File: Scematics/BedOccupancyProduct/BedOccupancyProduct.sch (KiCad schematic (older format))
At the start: 6 parts

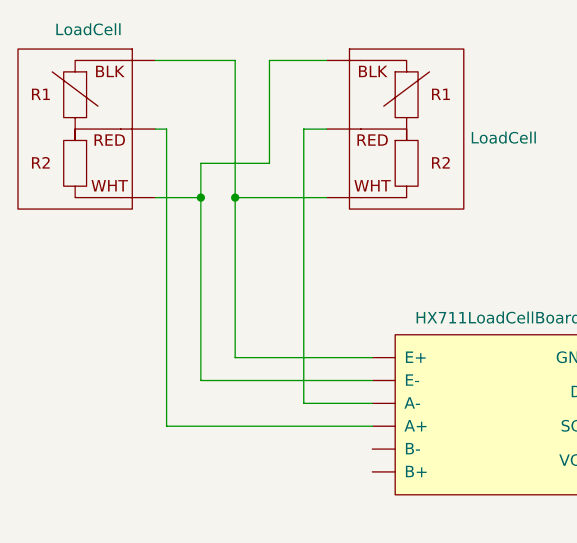
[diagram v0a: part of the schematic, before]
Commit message: code for initial timer and snooze control
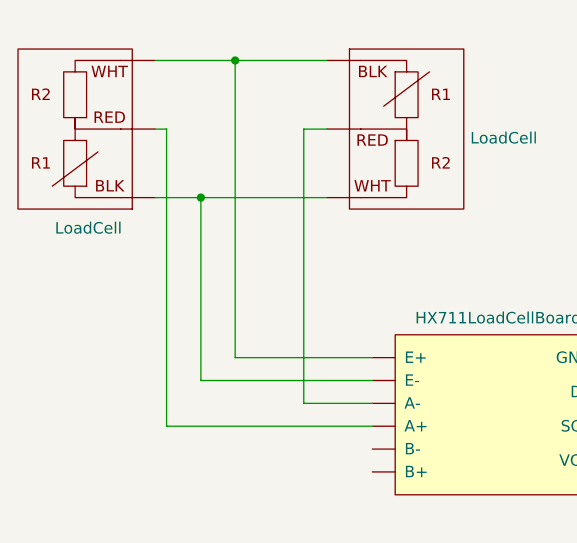
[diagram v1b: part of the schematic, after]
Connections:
- wire segments 39 -> 35
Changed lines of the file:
@@
 $EndComp
-Wire Wire Line
-	1800 1100 2150 1100
-Wire Wire Line
-	2150 1100 2150 1700
-Wire Wire Line
-	2150 1700 2550 1700
-Wire Wire Line
-	2550 1100 2300 1100
-Wire Wire Line
-	2300 1100 2300 1550
-Wire Wire Line
-	2300 1550 2000 1550
-Wire Wire Line
-	2000 1550 2000 1700
-Wire Wire Line
-	2000 1700 1800 1700
-Connection ~ 2000 1700
-Connection ~ 2150 1700
 Wire Wire Line
 	2550 1400 2450 1400
@@
 L alarmclocksystem:LoadCell U?
 U 1 1 5FA06464
-P 1350 900
-F 0 "U?" H 1192 925 50  0001 C CNN
-F 1 "LoadCell" H 1192 834 50  0000 C CNN
-F 2 "" H 1350 900 50  0001 C CNN
-F 3 "" H 1350 900 50  0001 C CNN
-	1    1350 900
-	-1   0    0    -1
+P 1350 1900
+F 0 "U?" H 1192 1925 50  0001 C CNN
+F 1 "LoadCell" H 1192 1834 50  0000 C CNN
+F 2 "" H 1350 1900 50  0001 C CNN
+F 3 "" H 1350 1900 50  0001 C CNN
+	1    1350 1900
+	-1   0    0    1
 $EndComp
 Wire Wire Line
@@
 	2750 2400 2150 2400
 Wire Wire Line
-	2150 1700 2150 2400
-Wire Wire Line
 	2750 2500 2000 2500
-Wire Wire Line
-	2000 1700 2000 2500
 Wire Wire Line
 	2750 2600 2450 2600
@@
 Wire Wire Line
 	6000 3050 7200 3050
+Wire Wire Line
+	1800 1100 2150 1100
+Wire Wire Line
+	1800 1700 2000 1700
+Wire Wire Line
+	2150 2400 2150 1100
+Connection ~ 2150 1100
+Wire Wire Line
+	2150 1100 2550 1100
+Wire Wire Line
+	2000 2500 2000 1700
+Connection ~ 2000 1700
+Wire Wire Line
+	2000 1700 2550 1700
 $EndSCHEMATC

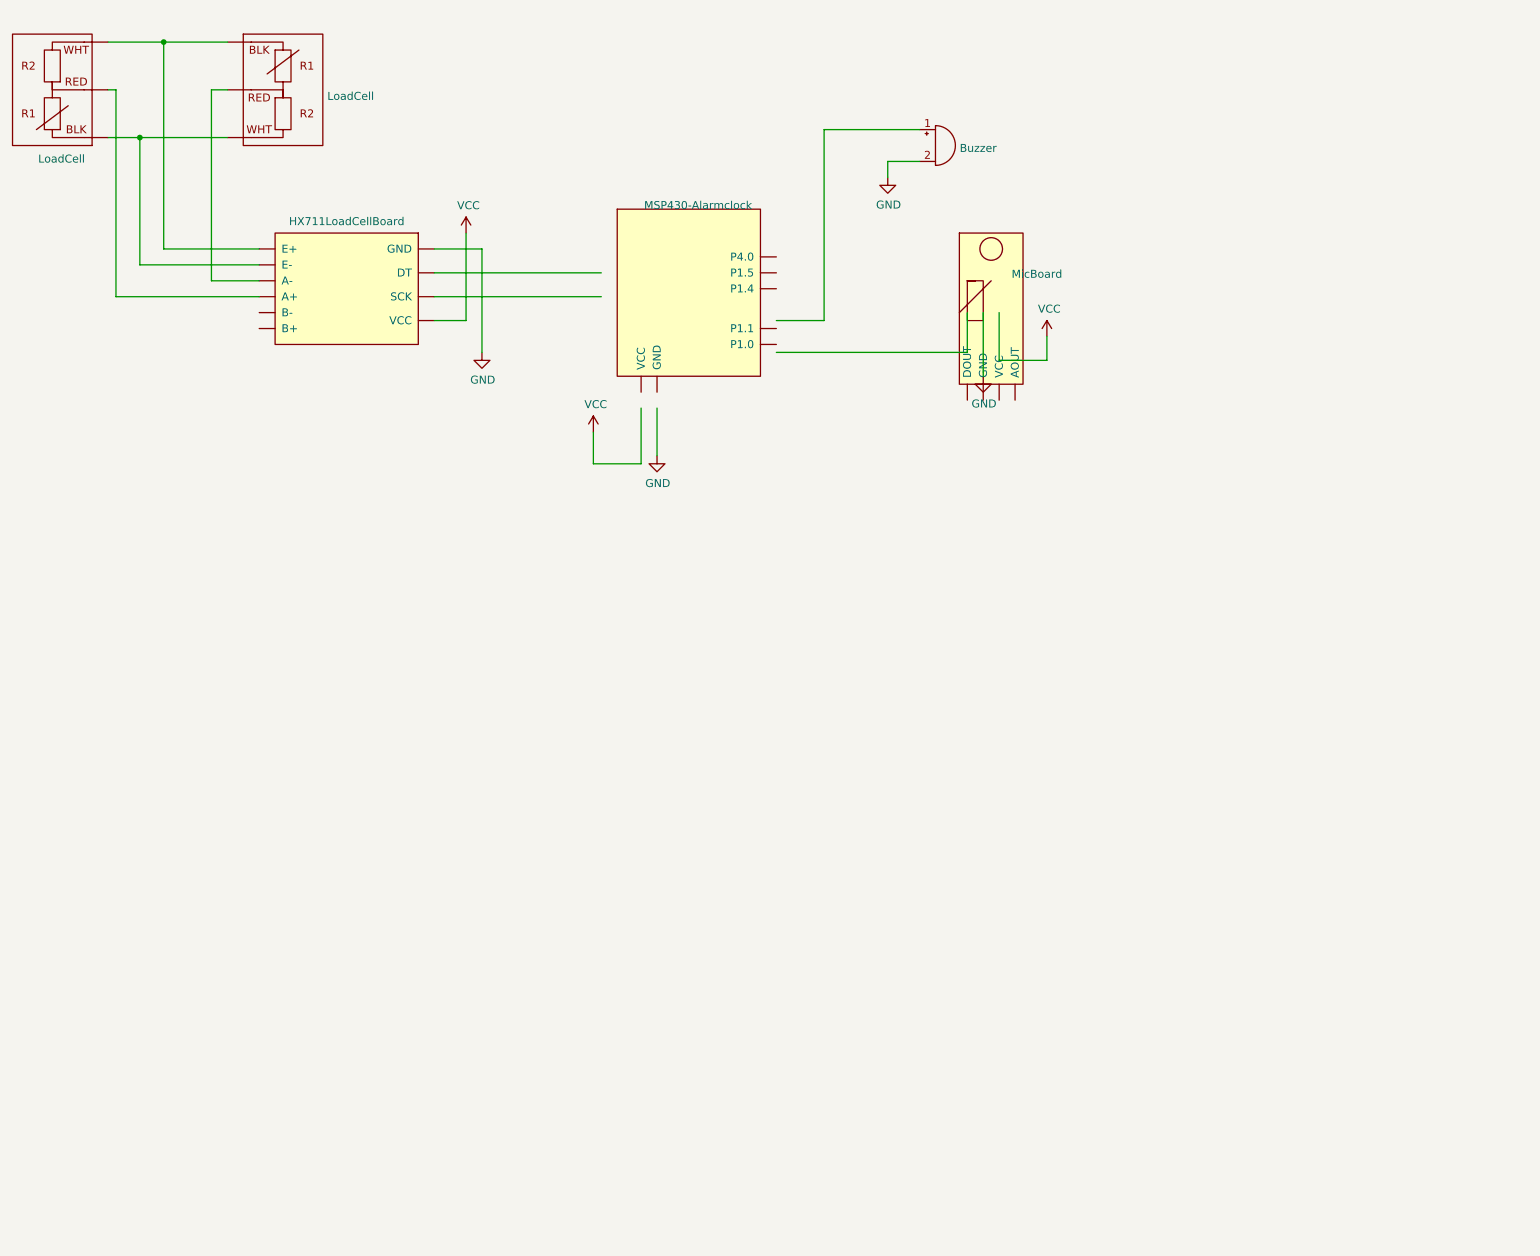
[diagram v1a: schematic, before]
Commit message: timers working with constant buzzer
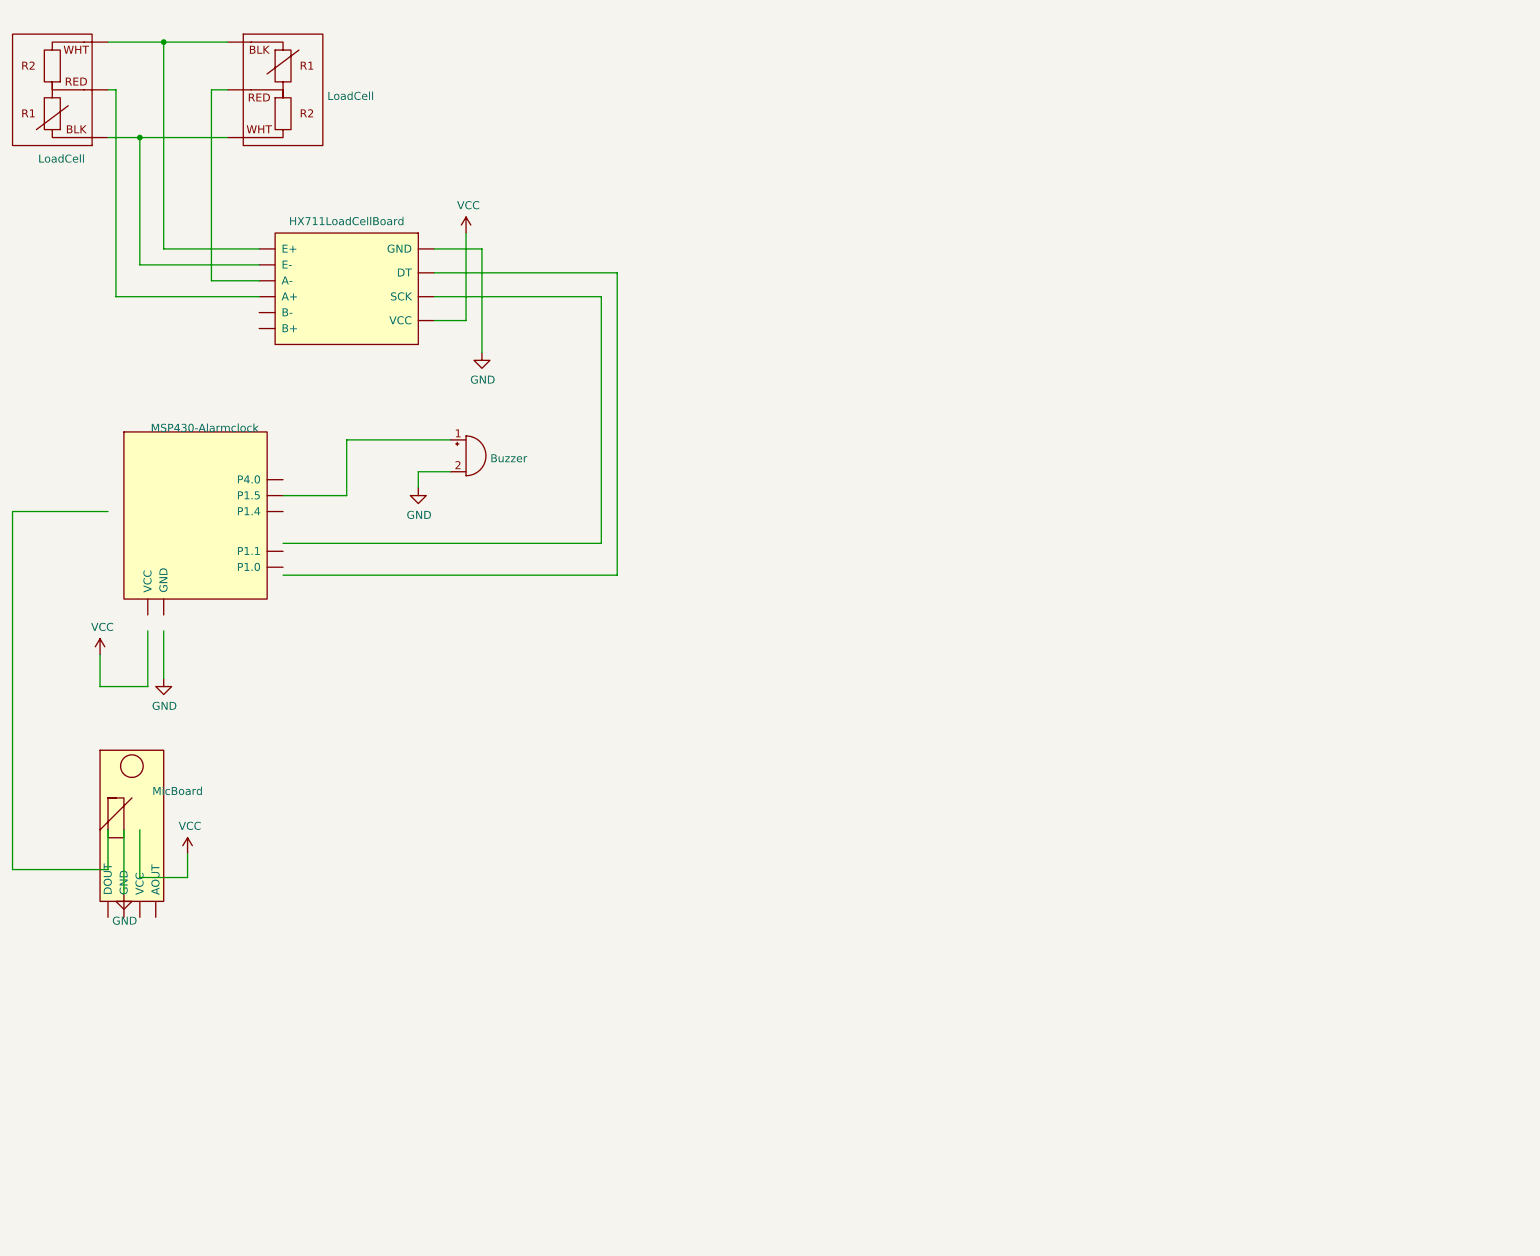
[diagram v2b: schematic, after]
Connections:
- wire segments 35 -> 41
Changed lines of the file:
@@
 L alarmclocksystem:MSP430-Alarmclock U?
 U 1 1 5FA0B0E4
-P 5450 2000
-F 0 "U?" H 5508 1965 50  0001 C CNN
-F 1 "MSP430-Alarmclock" H 5508 1874 50  0000 C CNN
-F 2 "" H 5450 2000 50  0001 C CNN
-F 3 "" H 5450 2000 50  0001 C CNN
-	1    5450 2000
+P 2350 3400
+F 0 "U?" H 2408 3365 50  0001 C CNN
+F 1 "MSP430-Alarmclock" H 2408 3274 50  0000 C CNN
+F 2 "" H 2350 3400 50  0001 C CNN
+F 3 "" H 2350 3400 50  0001 C CNN
+	1    2350 3400
 	1    0    0    -1
 $EndComp
@@
 L Device:Buzzer BZ?
 U 1 1 5FA05A32
-P 7000 1750
-F 0 "BZ?" H 7152 1779 50  0001 L CNN
-F 1 "Buzzer" H 7152 1733 50  0000 L CNN
-F 2 "" V 6975 1850 50  0001 C CNN
-F 3 "~" V 6975 1850 50  0001 C CNN
-	1    7000 1750
+P 4050 3700
+F 0 "BZ?" H 4202 3729 50  0001 L CNN
+F 1 "Buzzer" H 4202 3683 50  0000 L CNN
+F 2 "" V 4025 3800 50  0001 C CNN
+F 3 "~" V 4025 3800 50  0001 C CNN
+	1    4050 3700
 	1    0    0    -1
 $EndComp
-Wire Wire Line
-	6000 2850 6300 2850
-Wire Wire Line
-	6300 2850 6300 1650
-Wire Wire Line
-	6300 1650 6900 1650
 $Comp
 L power:GND #PWR?
 U 1 1 5FA08032
-P 5250 3700
-F 0 "#PWR?" H 5250 3450 50  0001 C CNN
-F 1 "GND" H 5255 3527 50  0000 C CNN
-F 2 "" H 5250 3700 50  0001 C CNN
-F 3 "" H 5250 3700 50  0001 C CNN
-	1    5250 3700
+P 2150 5100
+F 0 "#PWR?" H 2150 4850 50  0001 C CNN
+F 1 "GND" H 2155 4927 50  0000 C CNN
+F 2 "" H 2150 5100 50  0001 C CNN
+F 3 "" H 2150 5100 50  0001 C CNN
+	1    2150 5100
 	1    0    0    -1
 $EndComp
@@
 L power:VCC #PWR?
 U 1 1 5FA0877C
-P 4850 3550
-F 0 "#PWR?" H 4850 3400 50  0001 C CNN
-F 1 "VCC" H 4865 3723 50  0000 C CNN
-F 2 "" H 4850 3550 50  0001 C CNN
-F 3 "" H 4850 3550 50  0001 C CNN
-	1    4850 3550
+P 1750 4950
+F 0 "#PWR?" H 1750 4800 50  0001 C CNN
+F 1 "VCC" H 1765 5123 50  0000 C CNN
+F 2 "" H 1750 4950 50  0001 C CNN
+F 3 "" H 1750 4950 50  0001 C CNN
+	1    1750 4950
 	1    0    0    -1
 $EndComp
 Wire Wire Line
-	5150 3400 5150 3750
+	2050 4800 2050 5150
 Wire Wire Line
-	5150 3750 4850 3750
+	2050 5150 1750 5150
 Wire Wire Line
-	4850 3750 4850 3550
+	1750 5150 1750 4950
 Wire Wire Line
-	5250 3400 5250 3700
+	2150 4800 2150 5100
 $Comp
 L power:GND #PWR?
 U 1 1 5FA0C681
-P 6700 1950
-F 0 "#PWR?" H 6700 1700 50  0001 C CNN
-F 1 "GND" H 6705 1777 50  0000 C CNN
-F 2 "" H 6700 1950 50  0001 C CNN
-F 3 "" H 6700 1950 50  0001 C CNN
-	1    6700 1950
+P 3750 3900
+F 0 "#PWR?" H 3750 3650 50  0001 C CNN
+F 1 "GND" H 3755 3727 50  0000 C CNN
+F 2 "" H 3750 3900 50  0001 C CNN
+F 3 "" H 3750 3900 50  0001 C CNN
+	1    3750 3900
 	1    0    0    -1
 $EndComp
 Wire Wire Line
-	6900 1850 6700 1850
+	3950 3800 3750 3800
 Wire Wire Line
-	6700 1850 6700 1950
+	3750 3800 3750 3900
 $Comp
 L power:GND #PWR?
@@
 Wire Wire Line
 	3850 2700 4900 2700
-Wire Wire Line
-	3850 2550 4900 2550
 $Comp
 L power:GND #PWR?
 U 1 1 5FA0C4CF
-P 7300 3200
-F 0 "#PWR?" H 7300 2950 50  0001 C CNN
-F 1 "GND" H 7305 3027 50  0000 C CNN
-F 2 "" H 7300 3200 50  0001 C CNN
-F 3 "" H 7300 3200 50  0001 C CNN
-	1    7300 3200
+P 1900 6450
+F 0 "#PWR?" H 1900 6200 50  0001 C CNN
+F 1 "GND" H 1905 6277 50  0000 C CNN
+F 2 "" H 1900 6450 50  0001 C CNN
+F 3 "" H 1900 6450 50  0001 C CNN
+	1    1900 6450
 	1    0    0    -1
 $EndComp
@@
 L power:VCC #PWR?
 U 1 1 5FA0BEB9
-P 7700 2950
-F 0 "#PWR?" H 7700 2800 50  0001 C CNN
-F 1 "VCC" H 7715 3123 50  0000 C CNN
-F 2 "" H 7700 2950 50  0001 C CNN
-F 3 "" H 7700 2950 50  0001 C CNN
-	1    7700 2950
+P 2300 6200
+F 0 "#PWR?" H 2300 6050 50  0001 C CNN
+F 1 "VCC" H 2315 6373 50  0000 C CNN
+F 2 "" H 2300 6200 50  0001 C CNN
+F 3 "" H 2300 6200 50  0001 C CNN
+	1    2300 6200
 	1    0    0    -1
 $EndComp
 Wire Wire Line
-	7700 3100 7700 2950
+	2300 6350 2300 6200
 Wire Wire Line
-	7400 3100 7700 3100
+	2000 6350 2300 6350
 Wire Wire Line
-	7400 2800 7400 3100
+	2000 6050 2000 6350
 Wire Wire Line
-	7300 2800 7300 3200
+	1900 6050 1900 6450
 $Comp
 L alarmclocksystem:MicBoard U?
 U 1 1 5FA05211
-P 7250 2200
-F 0 "U?" H 7478 1888 50  0001 L CNN
-F 1 "MicBoard" H 7478 1842 50  0000 L CNN
-F 2 "" H 7250 2300 50  0001 C CNN
-F 3 "" H 7250 2300 50  0001 C CNN
-	1    7250 2200
+P 1850 5450
+F 0 "U?" H 2078 5138 50  0001 L CNN
+F 1 "MicBoard" H 2078 5092 50  0000 L CNN
+F 2 "" H 1850 5550 50  0001 C CNN
+F 3 "" H 1850 5550 50  0001 C CNN
+	1    1850 5450
 	1    0    0    -1
 $EndComp
 Wire Wire Line
-	7200 2800 7200 3050
-Wire Wire Line
-	6000 3050 7200 3050
+	1800 6050 1800 6300
 Wire Wire Line
 	1800 1100 2150 1100
@@
 Wire Wire Line
 	2000 1700 2550 1700
+Wire Wire Line
+	4900 2700 4900 4250
+Wire Wire Line
+	4900 4250 2900 4250
+Wire Wire Line
+	5000 2550 5000 4450
+Wire Wire Line
+	5000 4450 2900 4450
+Wire Wire Line
+	3850 2550 5000 2550
+Wire Wire Line
+	1800 4050 1200 4050
+Wire Wire Line
+	1200 4050 1200 6300
+Wire Wire Line
+	1200 6300 1800 6300
+Wire Wire Line
+	2900 3950 3300 3950
+Wire Wire Line
+	3300 3950 3300 3600
+Wire Wire Line
+	3300 3600 3950 3600
 $EndSCHEMATC

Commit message: schematc update
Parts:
- removed BZ?: Buzzer, symbol Device:Buzzer
- added SW?: SW_Push, symbol Switch:SW_Push
- added U?: PassiveBuzzerBoard, symbol alarmclocksystem:PassiveBuzzerBoard
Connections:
- net labels added: BUZZ, CLK, LOAD, MIC
- wire segments 41 -> 40

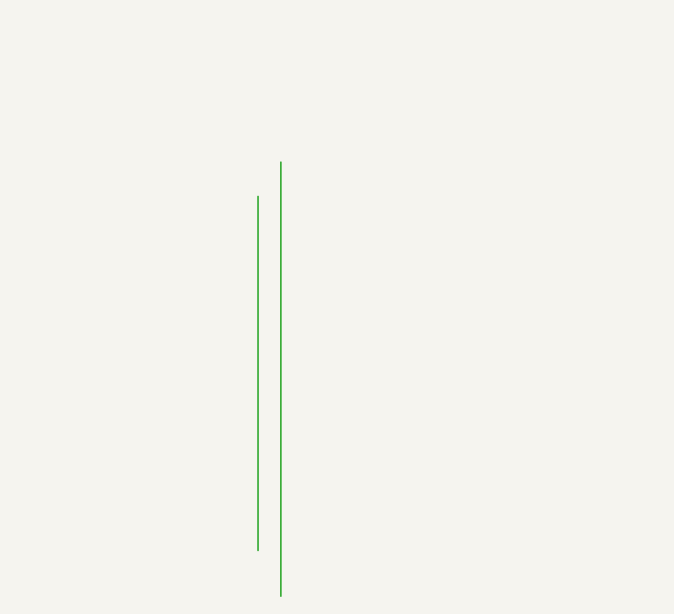
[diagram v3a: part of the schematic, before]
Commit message: schematic made smaller
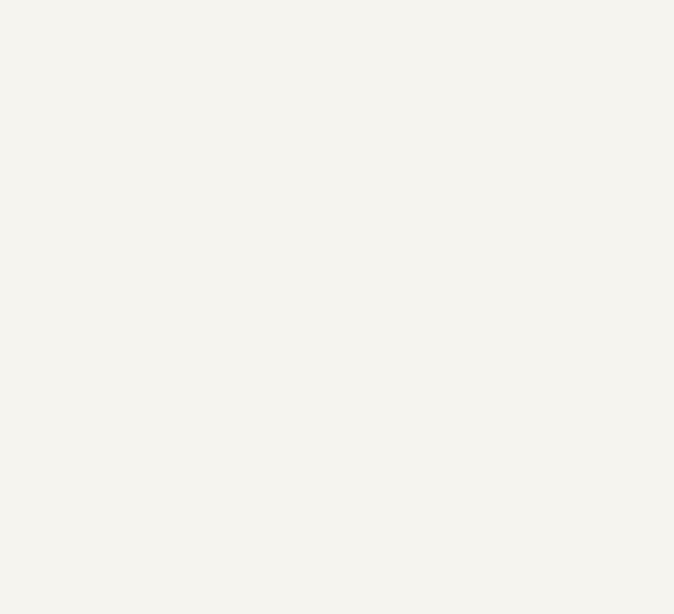
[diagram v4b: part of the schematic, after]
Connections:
- wire segments 40 -> 38
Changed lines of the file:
@@
 	6300 4200 6850 4200
-Wire Wire Line
-	6550 6900 6550 8450
-Wire Wire Line
-	6650 6750 6650 8650
 Wire Wire Line
 	8150 5050 9300 5050
